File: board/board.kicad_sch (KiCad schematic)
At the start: 1 part

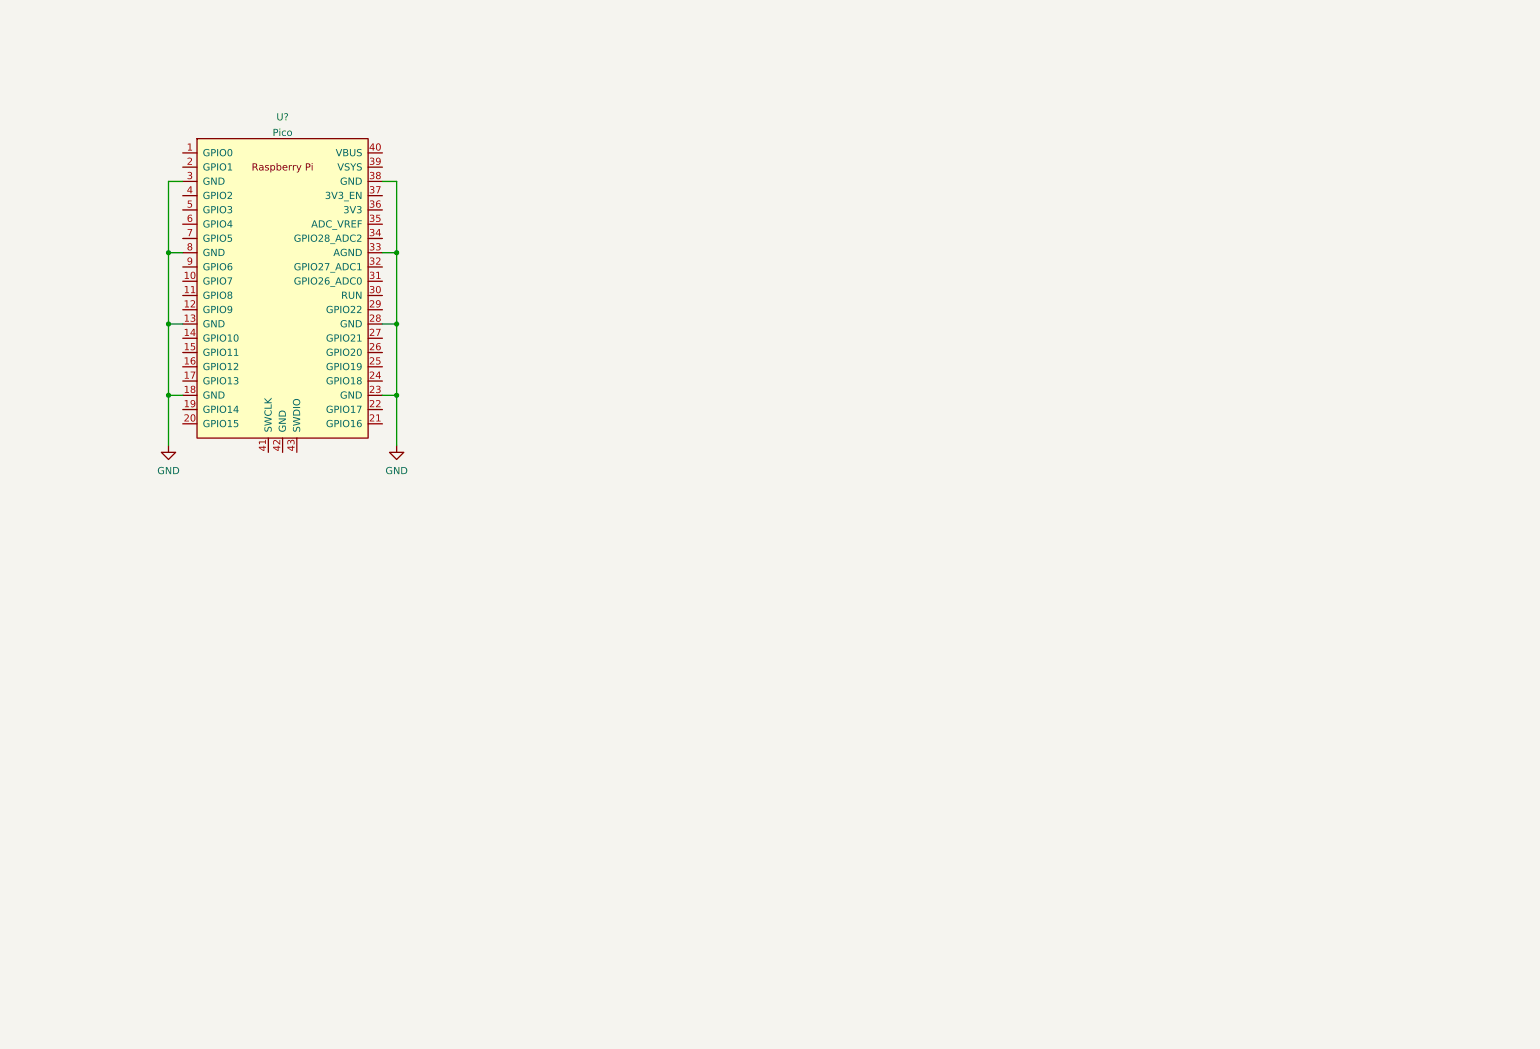
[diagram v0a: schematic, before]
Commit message: Schema with power section and start of cpu dac interface
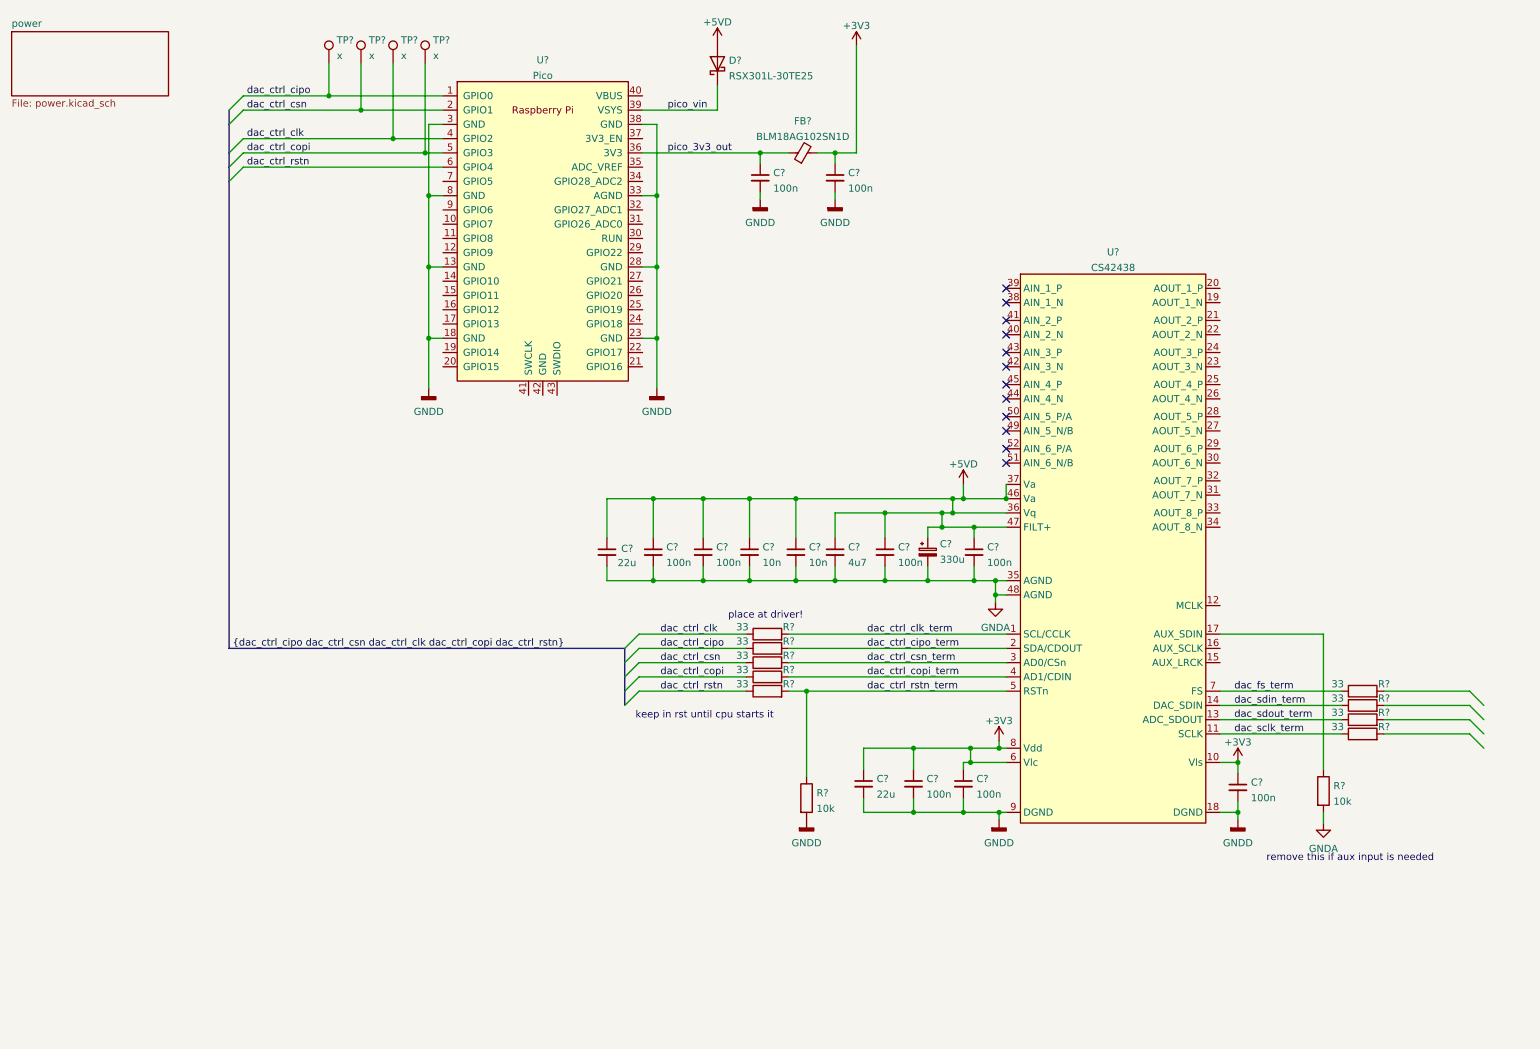
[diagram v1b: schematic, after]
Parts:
- added C? (x9): 100n, Capacitor_SMD:C_0603_1608Metric_Pad1.08x0.95mm_HandSolder, symbol Device:C_Small
- added C? (x2): 10n, Capacitor_SMD:C_0603_1608Metric_Pad1.08x0.95mm_HandSolder, symbol Device:C_Small
- added C?: 4u7, Capacitor_SMD:C_0603_1608Metric_Pad1.08x0.95mm_HandSolder, symbol Device:C_Small
- added C? (x2): 22u, Capacitor_SMD:C_0603_1608Metric_Pad1.08x0.95mm_HandSolder, symbol Device:C_Small
- added C?: 330u, symbol Device:C_Polarized_Small
- added D?: RSX301L-30TE25, symbol Device:D_Schottky
- added FB?: BLM18AG102SN1D, Inductor_SMD:L_0603_1608Metric_Pad1.05x0.95mm_HandSolder, symbol Device:FerriteBead_Small
- added R? (x9): 33, Resistor_SMD:R_0603_1608Metric_Pad0.98x0.95mm_HandSolder, symbol Device:R
- added R? (x2): 10k, Resistor_SMD:R_0603_1608Metric_Pad0.98x0.95mm_HandSolder, symbol Device:R
- added TP? (x4): x, TestPoint:TestPoint_Pad_D2.5mm, symbol Connector:TestPoint
- added U?: CS42438, Package_QFP:LQFP-52_10x10mm_P0.65mm, symbol good_things:CS42438
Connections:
- net dac_ctrl_cipo: now reaches U?.1 (GPIO0)
- net dac_ctrl_cipo: now also R?.1, TP?.1
- net dac_ctrl_csn: now reaches U?.2 (GPIO1)
- net dac_ctrl_csn: now also R?.1, TP?.1
- net pico_3v3_out: now reaches U?.36 (3V3)
- net pico_3v3_out: now also C?.1, FB?.1
- net pico_vin: now reaches U?.39 (VSYS)
- net pico_vin: now also D?.1 (K)
- net dac_ctrl_clk: now reaches U?.4 (GPIO2)
- net dac_ctrl_clk: now also R?.1, TP?.1
- net dac_ctrl_copi: now reaches U?.5 (GPIO3)
- net dac_ctrl_copi: now also R?.1, TP?.1
- net dac_ctrl_rstn: now reaches U?.6 (GPIO4)
- net dac_ctrl_rstn: now also R?.1
- net GND renamed GNDD
- net GNDD: now also C?.2, C?.2, C?.2, C?.2, C?.2, C?.2, R?.2, U?.18 (DGND), U?.9 (DGND)
- new net: R?.1, U?.17 (AUX_SDIN)
- new net +3V3: C?.1, C?.1, C?.1, C?.1, C?.1, FB?.2, U?.10 (Vls), U?.6 (Vlc), U?.8 (Vdd)
- new net +5VD: C?.1, C?.1, C?.1, C?.1, C?.1, C?.1, C?.1, C?.1, C?.1, D?.2 (A), U?.36 (Vq), U?.37 (Va), U?.46 (Va), U?.47 (FILT+)
- new net GNDA: C?.2, C?.2, C?.2, C?.2, C?.2, C?.2, C?.2, C?.2, C?.2, R?.2, U?.35 (AGND), U?.48 (AGND)
- new net dac_ctrl_cipo_term: R?.2, U?.2 (SDA/CDOUT)
- new net dac_ctrl_clk_term: R?.2, U?.1 (SCL/CCLK)
- new net dac_ctrl_copi_term: R?.2, U?.4 (AD1/CDIN)
- new net dac_ctrl_csn_term: R?.2, U?.3 (AD0/CSn)
- new net dac_ctrl_rstn_term: R?.1, R?.2, U?.5 (RSTn)
- new net dac_fs_term: R?.1, U?.7 (FS)
- new net dac_sclk_term: R?.1, U?.11 (SCLK)
- new net dac_sdin_term: R?.1, U?.14 (DAC_SDIN)
- new net dac_sdout_term: R?.1, U?.13 (ADC_SDOUT)
- no-connect marks 0 -> 12
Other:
- added sheet power (power.kicad_sch)
- note added: "keep in rst until cpu starts it"
- note added: "place at driver!"
- note added: "remove this if aux input is needed"
- moved on the sheet: U?

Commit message: schema for test of dac done
start layout
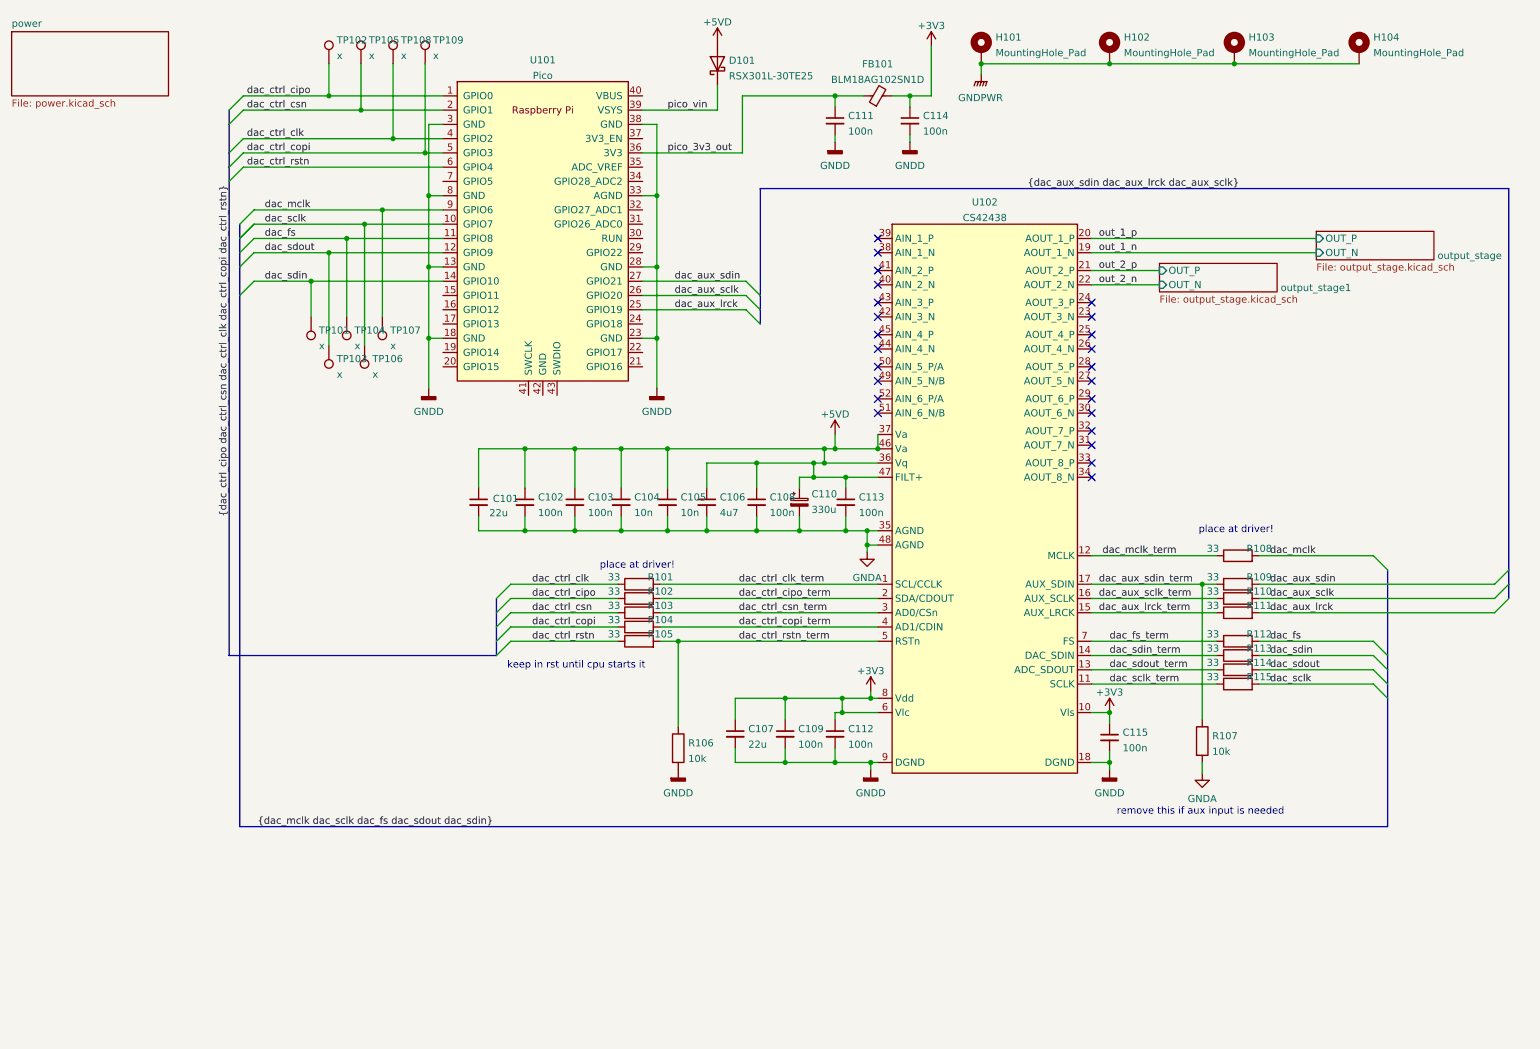
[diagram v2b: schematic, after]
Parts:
- added H101, H102, H103, H104: MountingHole_Pad, MountingHole:MountingHole_3.2mm_M3_ISO7380_Pad, symbol Mechanical:MountingHole_Pad
- added R108, R109, R110, R111: 33, Resistor_SMD:R_0603_1608Metric_Pad0.98x0.95mm_HandSolder, symbol Device:R
- added TP101, TP103, TP104, TP106, TP107: x, TestPoint:TestPoint_Pad_D2.5mm, symbol Connector:TestPoint
- D101: renamed from D?; footprint (none) -> good_things:SOD-106
- U101: renamed from U?; footprint RPi_Pico:RPi_Pico_SMD_TH -> MCU_RaspberryPi_and_Boards:RPi_Pico_SMD_TH
- gave numbers to parts that had none: 32
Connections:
- net dac_sclk: now reaches U101.10 (GPIO7)
- net dac_sclk: now also R115.2, TP106.1
- net dac_fs: now reaches U101.11 (GPIO8)
- net dac_fs: now also R112.2, TP104.1
- net dac_sdout: now reaches U101.12 (GPIO9)
- net dac_sdout: now also R114.2, TP103.1
- net dac_sdin: now reaches U101.14 (GPIO10)
- net dac_sdin: now also R113.2, TP101.1
- net dac_aux_lrck: now reaches U101.25 (GPIO19)
- net dac_aux_lrck: now also R111.2
- net dac_aux_sclk: now reaches U101.26 (GPIO20)
- net dac_aux_sclk: now also R110.2
- net dac_aux_sdin: now reaches U101.27 (GPIO21)
- net dac_aux_sdin: now also R109.2
- net dac_mclk: now reaches U101.9 (GPIO6)
- net dac_mclk: now also R108.2, TP107.1
- net dac_mclk_term: now reaches U102.12 (MCLK)
- net dac_mclk_term: now also R108.1
- net dac_aux_lrck_term: now reaches U102.15 (AUX_LRCK)
- net dac_aux_lrck_term: now also R111.1
- net dac_aux_sclk_term: now reaches U102.16 (AUX_SCLK)
- net dac_aux_sclk_term: now also R110.1
- net dac_aux_sdin_term: now reaches R107.1, U102.17 (AUX_SDIN)
- net dac_aux_sdin_term: now also R109.1
- net out_1_n: now reaches U102.19 (AOUT_1_N)
- net out_1_p: now reaches U102.20 (AOUT_1_P)
- net out_2_p: now reaches U102.21 (AOUT_2_P)
- net out_2_n: now reaches U102.22 (AOUT_2_N)
- new net GNDPWR: H101.1, H102.1, H103.1, H104.1
- no-connect marks 12 -> 24
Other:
- added sheet output_stage (output_stage.kicad_sch)
- added sheet output_stage1 (output_stage.kicad_sch)
- moved on the sheet: C101, C102, C103, C104, C105, C106, C107, C108, C109, C110, C111, C112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

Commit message: some layout
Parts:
- removed TP101: x, TestPoint:TestPoint_Pad_D2.5mm, symbol Connector:TestPoint
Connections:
- net GNDA: no longer R107.2
- net GNDD: now also R107.2
- net out_1_n renamed out_1_N
- net out_1_p renamed out_1_P
- net out_2_n renamed out_2_N
- net out_2_p renamed out_2_P
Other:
- note added: "accidental nazi"
- note added: "remember to set the invert channel 1 register bit 1 addr 0x10"

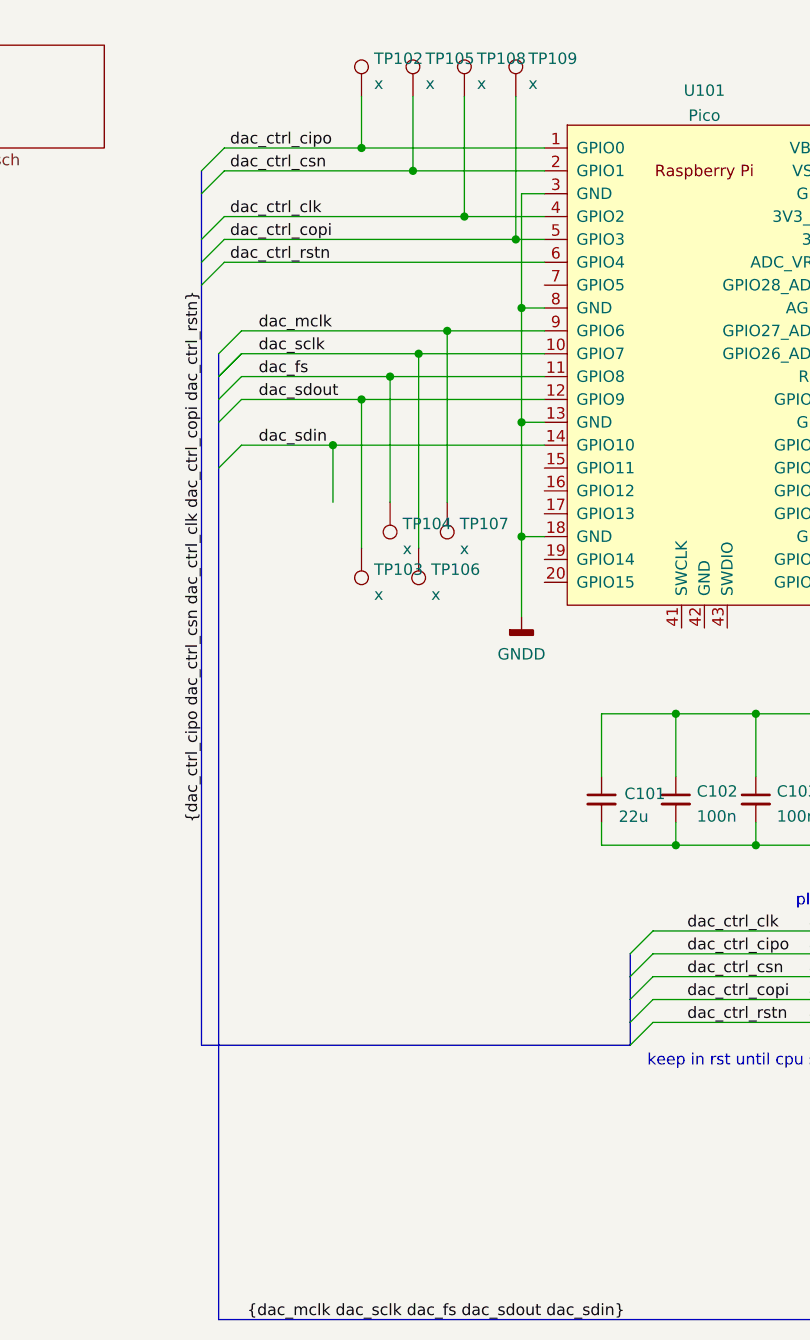
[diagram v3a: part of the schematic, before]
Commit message: Some more layout, digital side has been reorganized
looking into single to diff conversion. with the biases
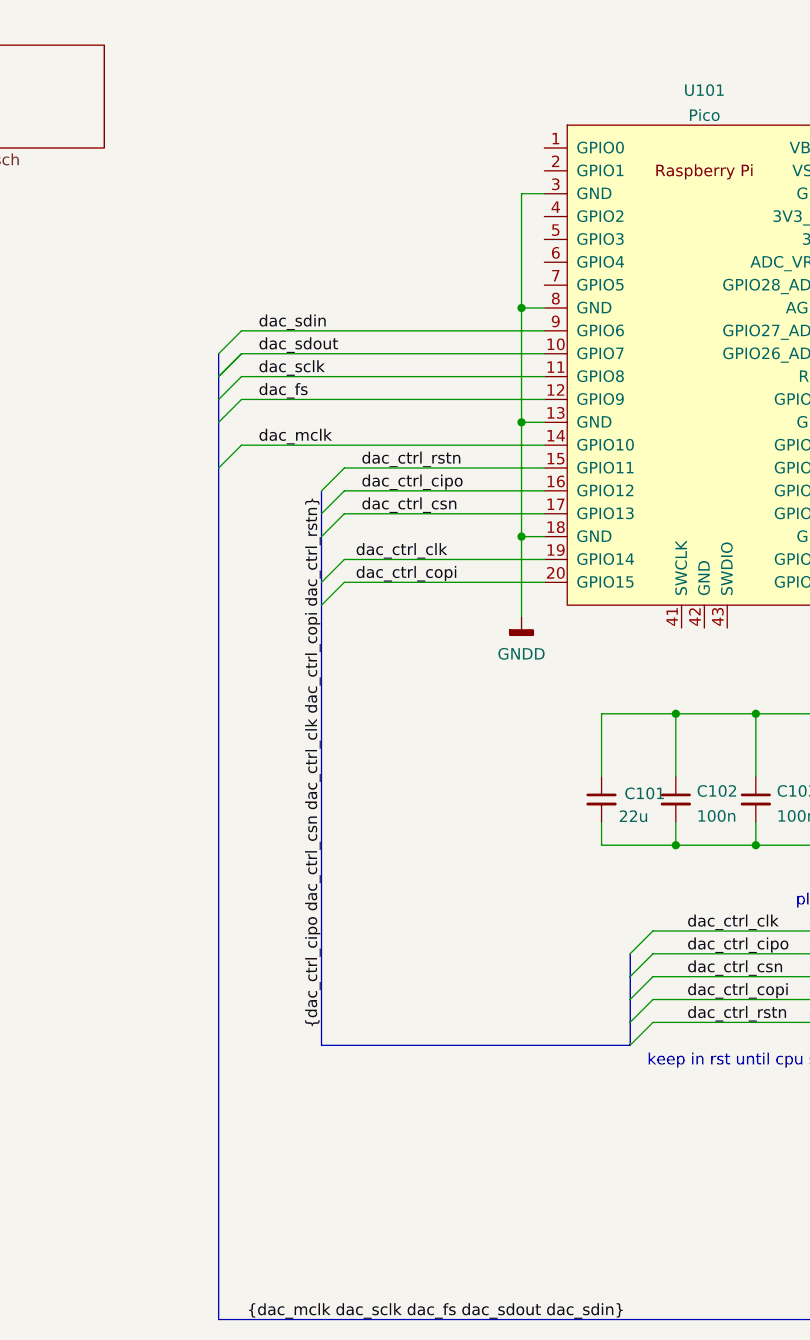
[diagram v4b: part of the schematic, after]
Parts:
- removed TP102, TP103, TP104, TP105, TP106, TP107, TP108, TP109: x, TestPoint:TestPoint_Pad_D2.5mm, symbol Connector:TestPoint
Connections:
- net dac_ctrl_cipo: now also U101.16 (GPIO12); no longer U101.1 (GPIO0)
- net dac_ctrl_clk: now also U101.19 (GPIO14); no longer U101.4 (GPIO2)
- net dac_ctrl_copi: now also U101.20 (GPIO15); no longer U101.5 (GPIO3)
- net dac_ctrl_csn: now also U101.17 (GPIO13); no longer U101.2 (GPIO1)
- net dac_ctrl_rstn: now also U101.15 (GPIO11); no longer U101.6 (GPIO4)
- net dac_fs: now also U101.12 (GPIO9); no longer U101.11 (GPIO8)
- net dac_mclk: now also U101.14 (GPIO10); no longer U101.9 (GPIO6)
- net dac_sclk: now also U101.11 (GPIO8); no longer U101.10 (GPIO7)
- net dac_sdin: now also U101.9 (GPIO6); no longer U101.14 (GPIO10)
- net dac_sdout: now also U101.10 (GPIO7); no longer U101.12 (GPIO9)

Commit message: some simerino
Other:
- added sheet a_input (a_input.kicad_sch)
- moved on the sheet: D101, U101
